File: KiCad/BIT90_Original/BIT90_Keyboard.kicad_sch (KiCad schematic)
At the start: 72 parts, among them SW1 MINUS, SW10 8, SW11 4, SW12 BS, SW13 DEL, SW14 2, SW15 6, SW16 ZERO, SW17 P, SW18 Y, SW19 W, SW2 7, SW20 ], SW21 UP, SW22 ESC, SW23 R, SW24 I, SW25 [, SW26 U, SW27 E, SW28 RUBOUT, SW29 RIGHT, SW3 3, SW30 Q, SW31 T, SW32 O, SW33 SEMICOLON, SW34 H, SW35 S, SW36 AT, SW37 FWDSLASH, SW38 CAPS/LOWER, SW39 F, SW4 BACKSLASH, SW40 K, SW41 COLON, SW42 J, SW43 D, SW44 CR, SW45 PERIOD, SW46 A, SW47 G, SW48 L, SW49 N, SW5 INS, SW50 V, SW51 X, SW52 M, SW53 COMMA, SW54 Z, SW55 C, SW56 B, SW57 SHIFT, SW58 BIT, SW59 BASIC, SW6 1, SW60 LEFT, SW61 DOWN, SW62 CTRL, SW63 SPACE, SW64 FCTN, SW7 5, SW8 6, SW9 CARAT, U30 74LS145, U31 74LS244, U32 74LS174

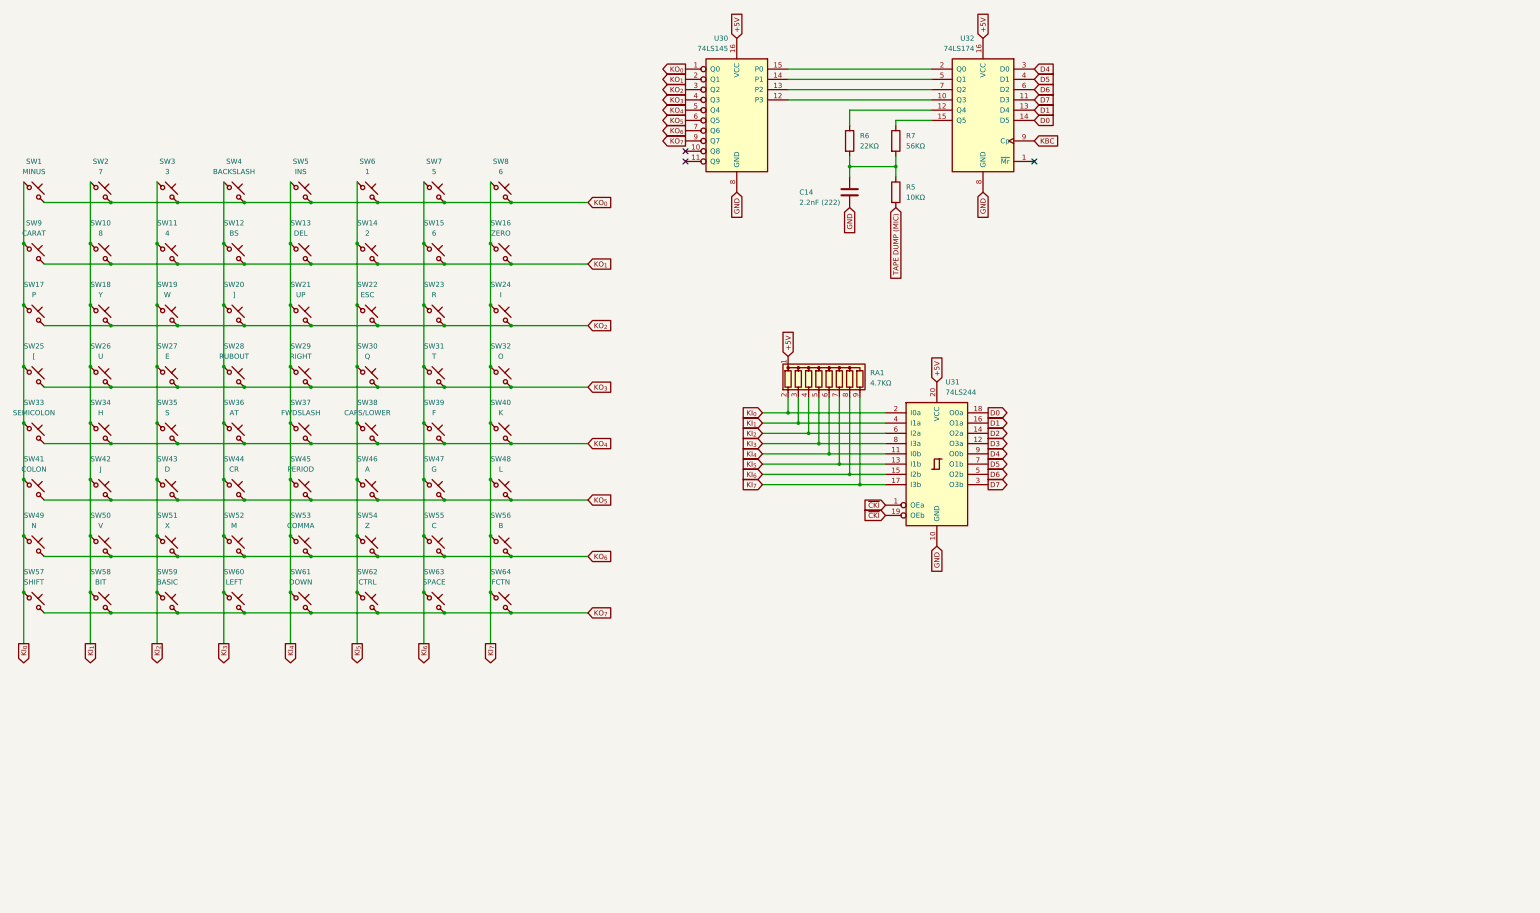
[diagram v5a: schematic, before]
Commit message: Completed original schematic redraw
Well, didn't finish the Video Encoder (PAL) sheet as I'm not going to use any of it in the new design.
Moved the audio output from that sheet to the Joystick/Audio/Tape out sheet where the sound generator is.
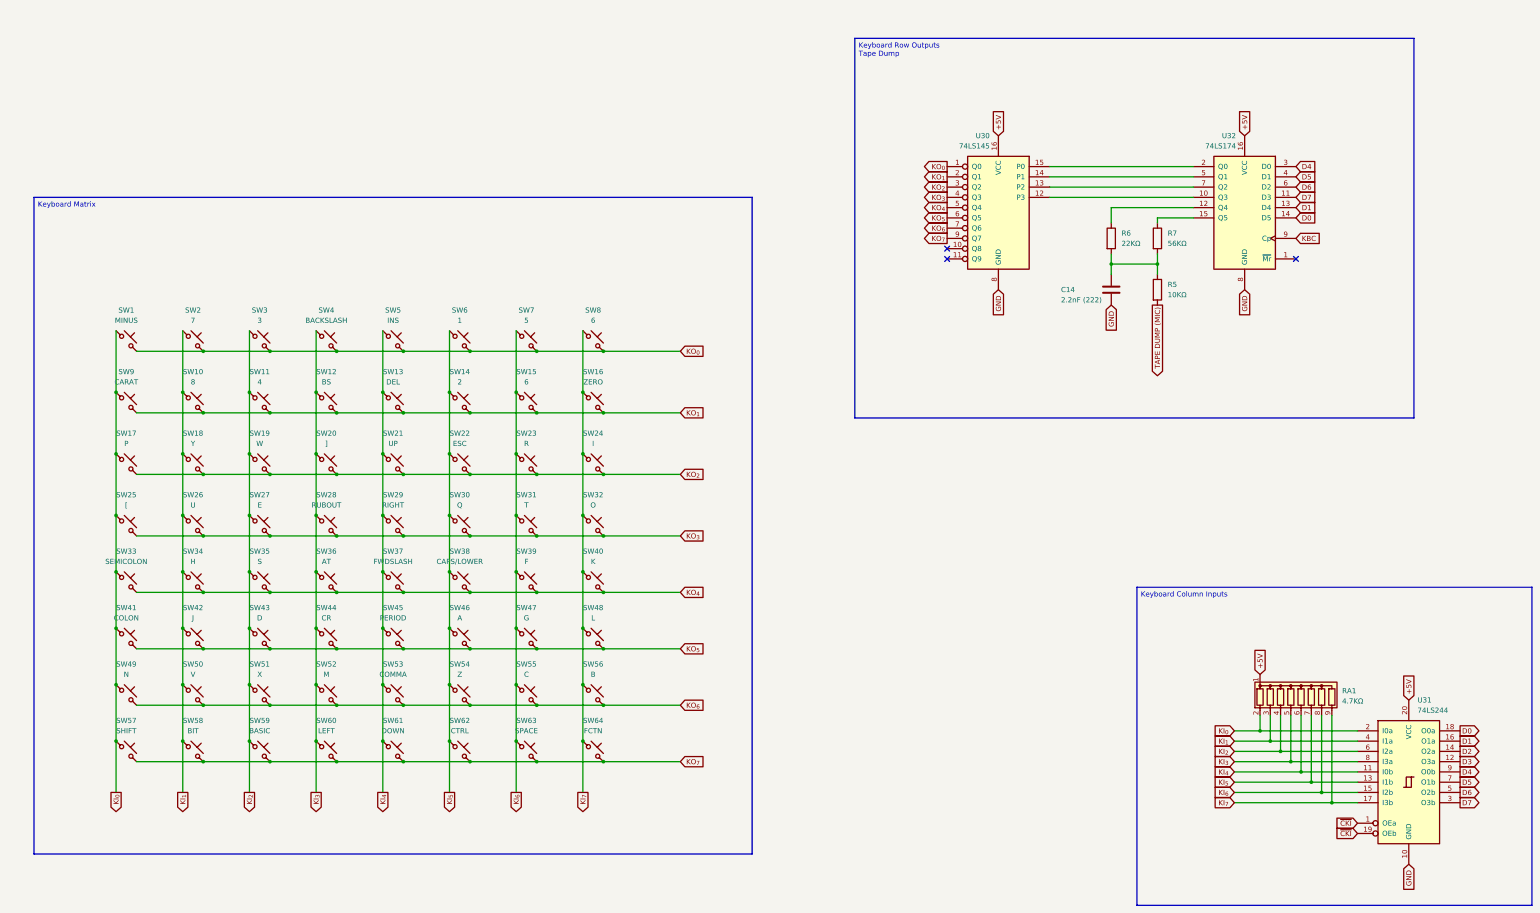
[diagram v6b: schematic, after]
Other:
- moved on the sheet: C14, R5, R6, R7, RA1, SW1, SW10, SW11, SW12, SW13, SW14, SW15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

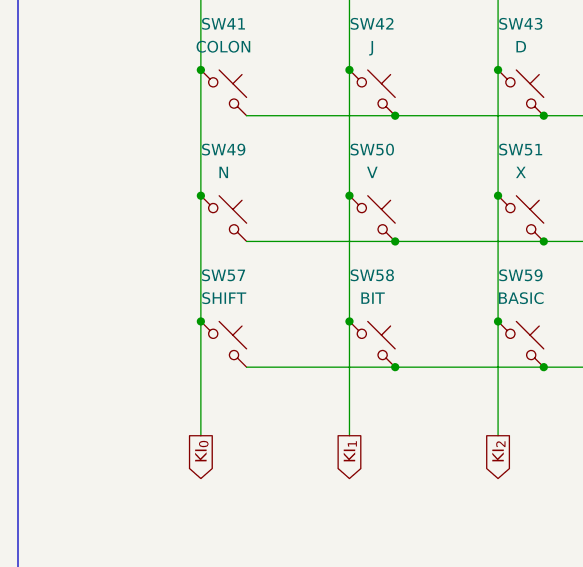
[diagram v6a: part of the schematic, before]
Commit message: Small updates/corrections
Managed to figure out some more errors/missing info from ColecoVision schematics & Henk's BIT90 motherboard underside photo
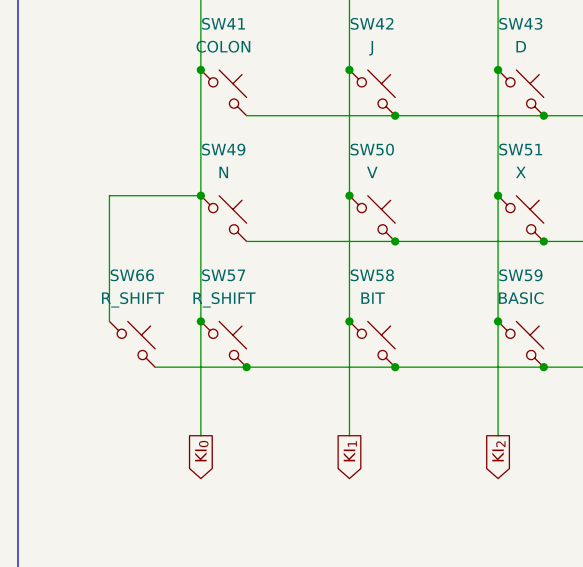
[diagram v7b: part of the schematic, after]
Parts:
- added SW66: R_SHIFT, symbol Switch:SW_Push_45deg
- SW57: value SHIFT -> R_SHIFT
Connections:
- net KI_{0}: now also SW66.1
- net KO_{7}: now also SW66.2
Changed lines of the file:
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@@
 	(title_block
 		(title "BIT90 Keyboard")
-		(date "4/JUN/2026")
+		(date "5/JUN/2026")
 		(rev "A")
 		(company "Brett Hallen")
@@
 	)
 	(junction
+		(at 49.53 201.93)
+		(diameter 0)
+		(color 0 0 0 0)
+	)
+	(junction
 		(at 127 168.91)
 		(diameter 0)
@@
 	(wire
 		(pts
+			(xy 34.29 182.88) (xy 34.29 196.85)
+		)
+		(stroke
+			(width 0)
+			(type default)
+		)
+	)
+	(wire
+		(pts
 			(xy 49.53 173.99) (xy 66.04 173.99)
 		)
@@
 	(wire
 		(pts
+			(xy 34.29 182.88) (xy 44.45 182.88)
+		)
+		(stroke
+			(width 0)
+			(type default)
+		)
+	)
+	(wire
+		(pts
 			(xy 77.47 110.49) (xy 77.47 125.73)
 		)
@@
 	(wire
 		(pts
+			(xy 39.37 201.93) (xy 49.53 201.93)
+		)
+		(stroke
+			(width 0)
+			(type default)
+		)
+	)
+	(wire
+		(pts
 			(xy 340.36 190.5) (xy 340.36 207.01)
 		)
@@
 	(symbol
 		(lib_id "Switch:SW_Push_45deg")
+		(at 36.83 199.39 0)
+		(unit 1)
+		(exclude_from_sim no)
+		(in_bom yes)
+		(on_board yes)
+		(dnp no)
+		(fields_autoplaced yes)
+		(property "Reference" "SW66"
+			(at 36.83 191.77 0)
+			(effects
+				(font
+					(size 1.27 1.27)
+				)
+			)
+		)
+		(property "Value" "R_SHIFT"
+			(at 36.83 194.31 0)
+			(effects
+				(font
+					(size 1.27 1.27)
+				)
+			)
+		)
+		(property "Footprint" ""
+			(at 36.83 199.39 0)
+			(effects
+				(font
+					(size 1.27 1.27)
+				)
+				(hide yes)
+			)
+		)
+		(property "Datasheet" "~"
+			(at 36.83 199.39 0)
+			(effects
+				(font
+					(size 1.27 1.27)
+				)
+				(hide yes)
+			)
+		)
+		(property "Description" "Push button switch, normally open, two pins, 45° tilted"
+			(at 36.83 199.39 0)
+			(effects
+				(font
+					(size 1.27 1.27)
+				)
+				(hide yes)
+			)
+		)
+		(pin "2"
+		)
+		(pin "1"
+		)
+		(instances
+			(project "BIT90_Original"
+				(path "/d65498c3-6385-4920-ac0f-4c76daf90780/7004f5d0-9464-4578-a2ed-1d5ed8c6edba"
+					(reference "SW66")
+					(unit 1)
+				)
+			)
+		)
+	)
+	(symbol
+		(lib_id "Switch:SW_Push_45deg")
 		(at 113.03 199.39 0)
 		(unit 1)
@@
 			)
 		)
-		(property "Value" "SHIFT"
+		(property "Value" "R_SHIFT"
 			(at 46.99 194.31 0)
 			(effects

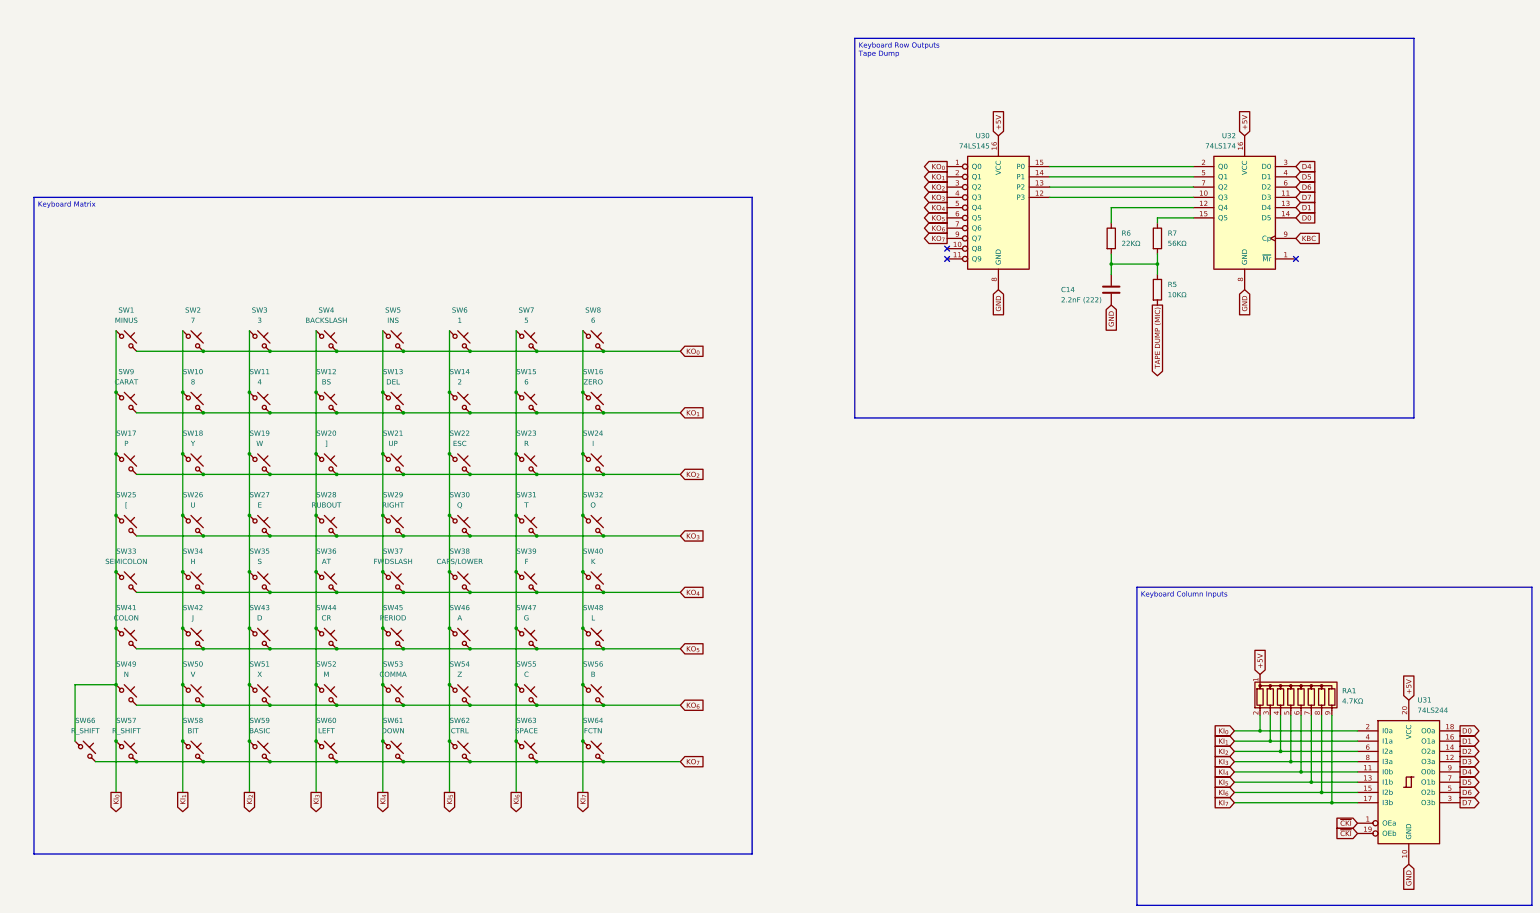
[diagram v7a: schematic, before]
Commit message: Resolved audio clock signal
Marked as EXTΦ on BIT90 schematic, generated via resistor from CPUΦ
Renamed it as AUDΦ so it's a bit clearer
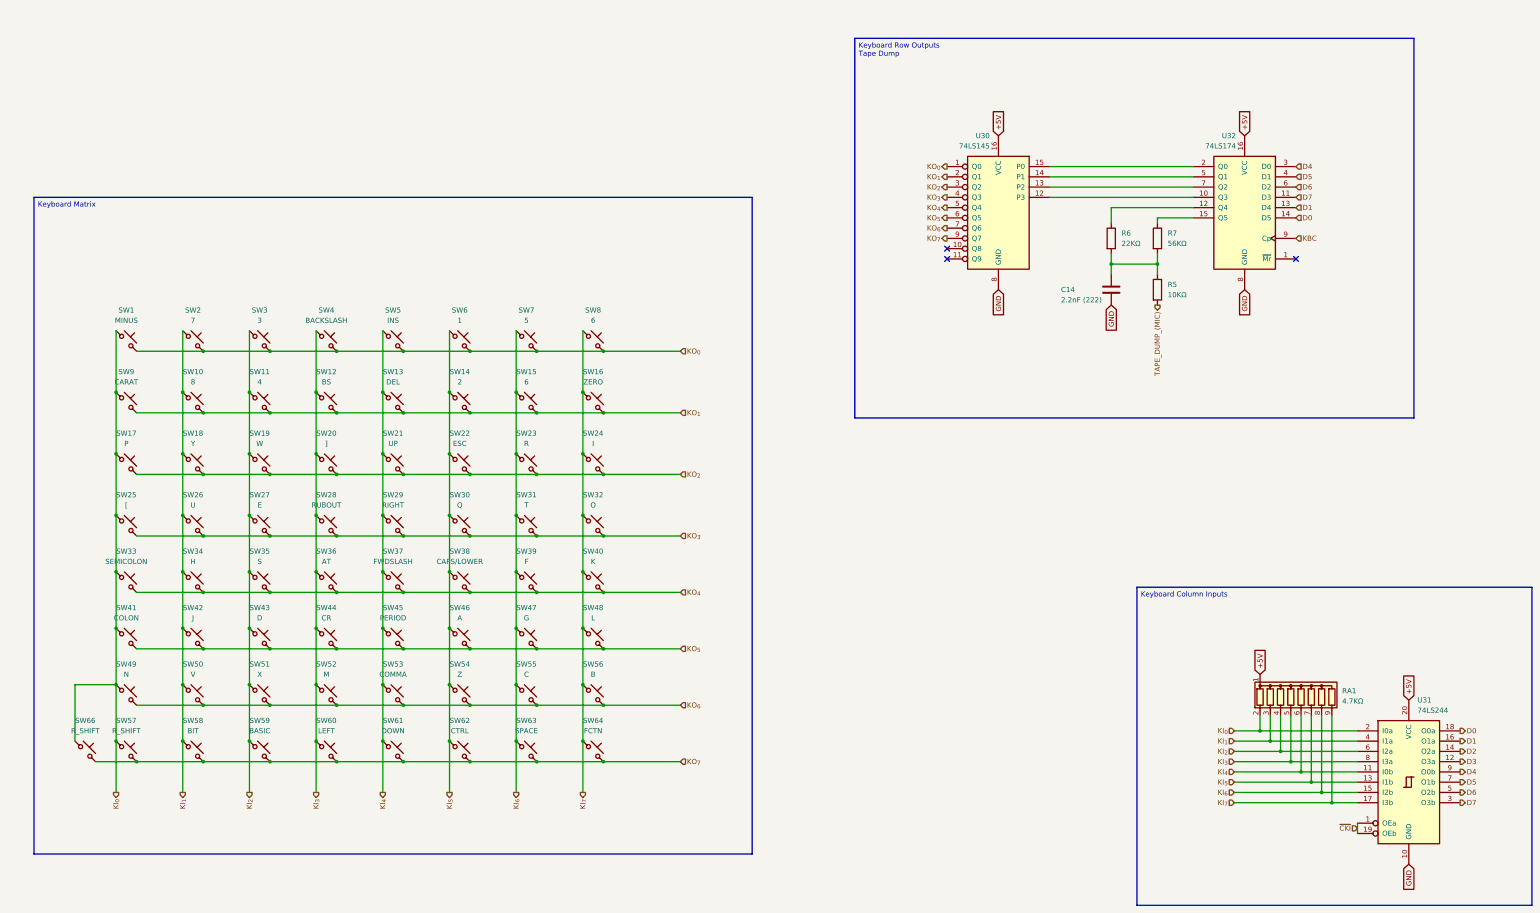
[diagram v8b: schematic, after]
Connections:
- net TAPE DUMP (MIC) renamed TAPE_DUMP_(MIC)
